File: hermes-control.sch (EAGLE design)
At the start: 73 parts, among them J1 1981568-1, J3 2201778-1, Q2 BC849SMD, Q3 FDN360P, Q4 FDN360P, Q5 BC849SMD, Q6 MMBT3906SOT23-3, Q7 FDN360P, Q8 MMBT2222A, U1 LSM9DS1TR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

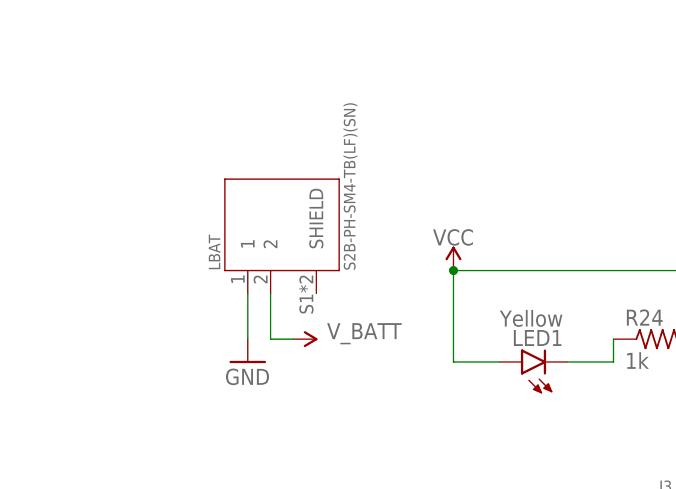
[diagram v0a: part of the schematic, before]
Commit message: new bat connector
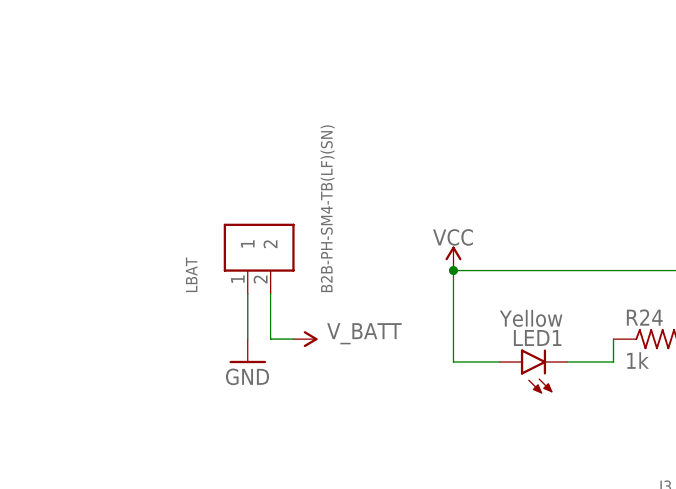
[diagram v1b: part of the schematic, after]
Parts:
- LBAT: value S2B-PH-SM4-TB(LF)(SN) -> B2B-PH-SM4-TB(LF)(SN); device hermes:S2B-PH-SM4-TB(LF)(SN) -> B2B-PH-SM4-TB_LF__SN_:B2B-PH-SM4-TB(LF)(SN)
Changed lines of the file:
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@@
 <part name="J3" library="hermes" deviceset="2201778-1" device=""/>
 <part name="GND13" library="supply1" library_urn="urn:adsk.eagle:library:371" deviceset="GND" device=""/>
-<part name="LBAT" library="hermes" deviceset="S2B-PH-SM4-TB(LF)(SN)" device=""/>
+<part name="LBAT" library="B2B-PH-SM4-TB_LF__SN_" deviceset="B2B-PH-SM4-TB(LF)(SN)" device=""/>
 <part name="SUPPLY22" library="SparkFun-PowerSymbols" library_urn="urn:adsk.eagle:library:530" deviceset="3.3V" device=""/>
 <part name="SUPPLY23" library="SparkFun-PowerSymbols" library_urn="urn:adsk.eagle:library:530" deviceset="3.3V" device=""/>
@@
 <attribute name="VALUE" x="124.46" y="106.68" size="1.778" layer="96"/>
 </instance>
-<instance part="LBAT" gate="G$1" x="50.8" y="172.72" smashed="yes" rot="R90">
-<attribute name="NAME" x="45.20428125" y="167.6371" size="1.272509375" layer="95" rot="R90"/>
-<attribute name="VALUE" x="60.22268125" y="167.63188125" size="1.275409375" layer="96" rot="R90"/>
+<instance part="LBAT" gate="G$1" x="48.26" y="170.18" smashed="yes" rot="R90">
+<attribute name="NAME" x="42.66428125" y="165.0971" size="1.272509375" layer="95" rot="R90"/>
+<attribute name="VALUE" x="57.68268125" y="165.09188125" size="1.275409375" layer="96" rot="R90"/>
 </instance>
 <instance part="SUPPLY22" gate="G$1" x="360.68" y="129.54" smashed="yes">

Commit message: flipped fet
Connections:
- net 3.3V: now also Q3.S; no longer Q3.D
- net N$6: now also Q3.D; no longer Q3.S
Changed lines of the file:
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@@
 <?xml version="1.0" encoding="utf-8"?>
 <!DOCTYPE eagle SYSTEM "eagle.dtd">
-<eagle version="9.4.0">
+<eagle version="9.4.2">
 <drawing>
 <settings>
@@
 <attribute name="VALUE" x="315.595" y="36.068" size="1.778" layer="96" rot="R90"/>
 </instance>
-<instance part="Q3" gate="G$1" x="236.22" y="30.48" smashed="yes" rot="R90">
-<attribute name="NAME" x="233.68" y="36.83" size="1.778" layer="95" rot="R90"/>
-<attribute name="VALUE" x="236.22" y="36.83" size="1.778" layer="96" rot="R90"/>
+<instance part="Q3" gate="G$1" x="236.22" y="30.48" smashed="yes" rot="MR90">
+<attribute name="NAME" x="238.76" y="36.83" size="1.778" layer="95" rot="MR90"/>
+<attribute name="VALUE" x="236.22" y="36.83" size="1.778" layer="96" rot="MR90"/>
 </instance>
 <instance part="C14" gate="G$1" x="218.44" y="30.48" smashed="yes">
@@
 <pinref part="SUPPLY7" gate="G$1" pin="3.3V"/>
 <wire x1="246.38" y1="35.56" x2="246.38" y2="33.02" width="0.1524" layer="91"/>
-<pinref part="Q3" gate="G$1" pin="D"/>
-<wire x1="246.38" y1="33.02" x2="241.3" y2="33.02" width="0.1524" layer="91"/>
+<pinref part="Q3" gate="G$1" pin="S"/>
+<wire x1="241.3" y1="33.02" x2="246.38" y2="33.02" width="0.1524" layer="91"/>
 </segment>
 <segment>
@@
 <pinref part="C7" gate="G$1" pin="1"/>
 <junction x="210.82" y="33.02"/>
-<pinref part="Q3" gate="G$1" pin="S"/>
+<pinref part="Q3" gate="G$1" pin="D"/>
 <wire x1="231.14" y1="33.02" x2="218.44" y2="33.02" width="0.1524" layer="91"/>
 <junction x="218.44" y="33.02"/>
@@
 </segment>
 <segment>
+<wire x1="238.76" y1="27.94" x2="248.92" y2="27.94" width="0.1524" layer="91"/>
+<label x="241.3" y="27.94" size="1.778" layer="95"/>
 <pinref part="Q3" gate="G$1" pin="G"/>
-<wire x1="233.68" y1="27.94" x2="248.92" y2="27.94" width="0.1524" layer="91"/>
-<label x="241.3" y="27.94" size="1.778" layer="95"/>
-</segment>
-</net>
+</segment>
+</net>

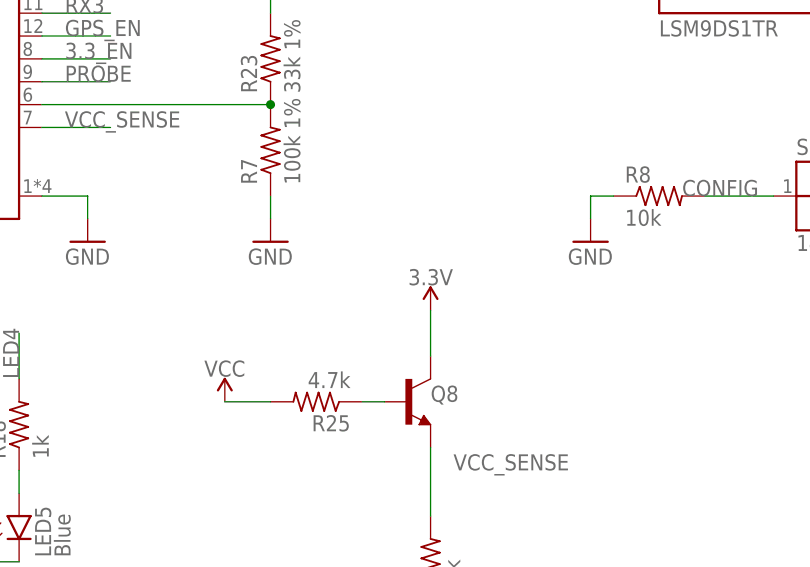
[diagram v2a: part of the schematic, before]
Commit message: changed from 3.3 to vccio
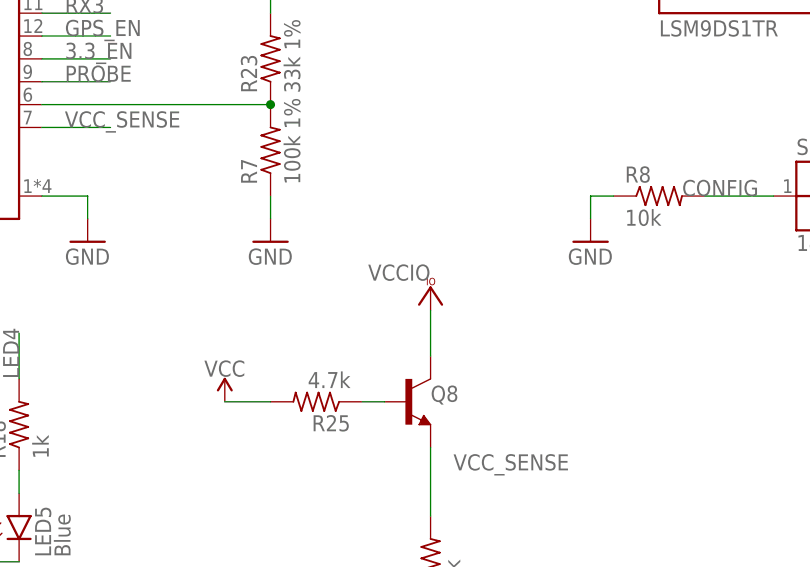
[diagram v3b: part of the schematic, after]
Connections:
- net 3.3V: no longer Q8.C
- net VCCIO: now also Q8.C
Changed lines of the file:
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@@
 <part name="R9" library="rcl" library_urn="urn:adsk.eagle:library:334" deviceset="R-US_" device="R0603" package3d_urn="urn:adsk.eagle:package:23555/3" value="10k"/>
 <part name="R25" library="rcl" library_urn="urn:adsk.eagle:library:334" deviceset="R-US_" device="R0603" package3d_urn="urn:adsk.eagle:package:23555/3" value="4.7k"/>
-<part name="SUPPLY31" library="SparkFun-PowerSymbols" library_urn="urn:adsk.eagle:library:530" deviceset="3.3V" device=""/>
 <part name="GND11" library="supply1" library_urn="urn:adsk.eagle:library:371" deviceset="GND" device=""/>
 <part name="VCC4" library="supply1" library_urn="urn:adsk.eagle:library:371" deviceset="VCCIO" device=""/>
 <part name="VCC5" library="supply1" library_urn="urn:adsk.eagle:library:371" deviceset="VCCIO" device=""/>
 <part name="VCC6" library="supply1" library_urn="urn:adsk.eagle:library:371" deviceset="VCCIO" device=""/>
+<part name="VCC7" library="supply1" library_urn="urn:adsk.eagle:library:371" deviceset="VCCIO" device=""/>
 </parts>
 <sheets>
@@
 <attribute name="VALUE" x="346.71" y="56.642" size="1.778" layer="96" rot="R180"/>
 </instance>
-<instance part="SUPPLY31" gate="G$1" x="355.6" y="63.5" smashed="yes">
-<attribute name="VALUE" x="355.6" y="66.294" size="1.778" layer="96" align="bottom-center"/>
-</instance>
 <instance part="GND11" gate="1" x="355.6" y="25.4" smashed="yes">
 <attribute name="VALUE" x="353.06" y="22.86" size="1.778" layer="96"/>
@@
 <instance part="VCC6" gate="G$1" x="129.54" y="147.32" smashed="yes">
 <attribute name="VALUE" x="129.54" y="149.86" size="1.778" layer="96" rot="R180"/>
+</instance>
+<instance part="VCC7" gate="G$1" x="355.6" y="66.04" smashed="yes">
+<attribute name="VALUE" x="355.6" y="68.58" size="1.778" layer="96" rot="R180"/>
 </instance>
 </instances>
@@
 <wire x1="228.6" y1="81.28" x2="228.6" y2="83.82" width="0.1524" layer="91"/>
 </segment>
-<segment>
-<pinref part="Q8" gate="&gt;NAME" pin="C"/>
-<pinref part="SUPPLY31" gate="G$1" pin="3.3V"/>
-<wire x1="355.6" y1="58.42" x2="355.6" y2="63.5" width="0.1524" layer="91"/>
-</segment>
 </net>
 <net name="N$4" class="0">
@@
 <wire x1="129.54" y1="139.7" x2="124.46" y2="139.7" width="0.1524" layer="91"/>
 </segment>
-</net>
+<segment>
+<pinref part="Q8" gate="&gt;NAME" pin="C"/>
+<wire x1="355.6" y1="58.42" x2="355.6" y2="63.5" width="0.1524" layer="91"/>
+<pinref part="VCC7" gate="G$1" pin="VCCIO"/>
+</segment>
+</net>

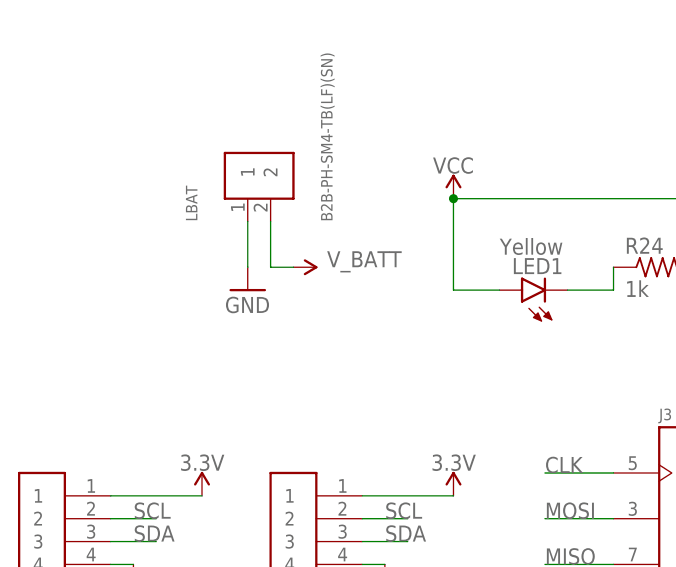
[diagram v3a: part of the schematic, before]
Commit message: changed batt connection
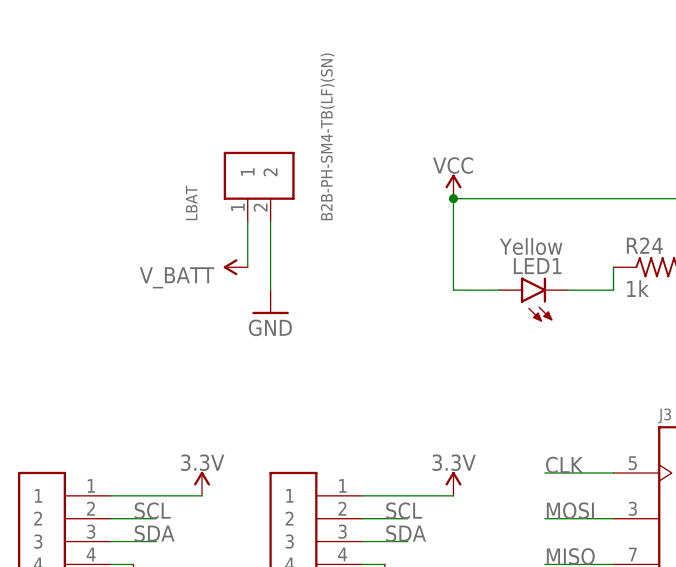
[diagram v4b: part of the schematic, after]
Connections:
- net GND: now also LBAT.2; no longer LBAT.1
- net V_BATT: now also LBAT.1; no longer LBAT.2
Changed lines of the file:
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@@
 <attribute name="VALUE" x="233.68" y="149.86" size="1.778" layer="96"/>
 </instance>
-<instance part="GND7" gate="1" x="48.26" y="157.48" smashed="yes">
-<attribute name="VALUE" x="45.72" y="154.94" size="1.778" layer="96"/>
-</instance>
-<instance part="SUPPLY6" gate="G$1" x="53.34" y="160.02" smashed="yes" rot="R270">
-<attribute name="VALUE" x="61.214" y="160.02" size="1.778" layer="96" align="bottom-center"/>
+<instance part="GND7" gate="1" x="50.8" y="154.94" smashed="yes">
+<attribute name="VALUE" x="48.26" y="152.4" size="1.778" layer="96"/>
+</instance>
+<instance part="SUPPLY6" gate="G$1" x="48.26" y="160.02" smashed="yes" rot="R90">
+<attribute name="VALUE" x="40.386" y="160.02" size="1.778" layer="96" rot="R180" align="bottom-center"/>
 </instance>
 <instance part="GND8" gate="1" x="200.66" y="17.78" smashed="yes">
@@
 </segment>
 <segment>
-<pinref part="GND7" gate="1" pin="GND"/>
-<wire x1="48.26" y1="160.02" x2="48.26" y2="165.1" width="0.1524" layer="91"/>
-<pinref part="LBAT" gate="G$1" pin="1"/>
-</segment>
-<segment>
 <pinref part="GND12" gate="1" pin="GND"/>
 <wire x1="147.32" y1="99.06" x2="147.32" y2="101.6" width="0.1524" layer="91"/>
@@
 <wire x1="129.54" y1="35.56" x2="137.16" y2="35.56" width="0.1524" layer="91"/>
 </segment>
+<segment>
+<pinref part="GND7" gate="1" pin="GND"/>
+<pinref part="LBAT" gate="G$1" pin="2"/>
+<wire x1="50.8" y1="157.48" x2="50.8" y2="165.1" width="0.1524" layer="91"/>
+</segment>
 </net>
 <net name="N$1" class="0">
@@
 </segment>
 <segment>
-<pinref part="SUPPLY6" gate="G$1" pin="V_BATT"/>
-<wire x1="53.34" y1="160.02" x2="50.8" y2="160.02" width="0.1524" layer="91"/>
-<wire x1="50.8" y1="160.02" x2="50.8" y2="165.1" width="0.1524" layer="91"/>
-<pinref part="LBAT" gate="G$1" pin="2"/>
-</segment>
-<segment>
 <pinref part="SUPPLY13" gate="G$1" pin="V_BATT"/>
 <wire x1="337.82" y1="99.06" x2="337.82" y2="96.52" width="0.1524" layer="91"/>
@@
 <wire x1="213.36" y1="172.72" x2="218.44" y2="172.72" width="0.1524" layer="91"/>
 </segment>
+<segment>
+<pinref part="SUPPLY6" gate="G$1" pin="V_BATT"/>
+<pinref part="LBAT" gate="G$1" pin="1"/>
+<wire x1="48.26" y1="160.02" x2="48.26" y2="165.1" width="0.1524" layer="91"/>
+</segment>
 </net>

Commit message: more vccio
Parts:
- added R5: 10k, rcl:R-US_R0603
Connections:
- net 3.3V: no longer R12.2, R13.2, S2.2
- net 3.3_EN: now also R5.1
- net VCCIO: now also R12.2, R13.2, R5.2, S2.2
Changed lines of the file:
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@@
 <?xml version="1.0" encoding="utf-8"?>
 <!DOCTYPE eagle SYSTEM "eagle.dtd">
-<eagle version="9.4.2">
+<eagle version="9.3.0">
 <drawing>
 <settings>
@@
 <part name="SUPPLY13" library="SparkFun-PowerSymbols" library_urn="urn:adsk.eagle:library:530" deviceset="V_BATT" device=""/>
 <part name="GND14" library="supply1" library_urn="urn:adsk.eagle:library:371" deviceset="GND" device=""/>
-<part name="SUPPLY14" library="SparkFun-PowerSymbols" library_urn="urn:adsk.eagle:library:530" deviceset="3.3V" device=""/>
 <part name="GND15" library="supply1" library_urn="urn:adsk.eagle:library:371" deviceset="GND" device=""/>
 <part name="U$3" library="BlueRobotics-JST-GH" deviceset="JST-GH-4" device="TOP"/>
@@
 <part name="R6" library="rcl" library_urn="urn:adsk.eagle:library:334" deviceset="R-US_" device="R0603" package3d_urn="urn:adsk.eagle:package:23555/3" value="1k"/>
 <part name="R12" library="rcl" library_urn="urn:adsk.eagle:library:334" deviceset="R-US_" device="R0603" package3d_urn="urn:adsk.eagle:package:23555/3" value="1k"/>
-<part name="SUPPLY26" library="SparkFun-PowerSymbols" library_urn="urn:adsk.eagle:library:530" deviceset="3.3V" device=""/>
 <part name="R13" library="rcl" library_urn="urn:adsk.eagle:library:334" deviceset="R-US_" device="R0603" package3d_urn="urn:adsk.eagle:package:23555/3" value="27k"/>
 <part name="R14" library="rcl" library_urn="urn:adsk.eagle:library:334" deviceset="R-US_" device="R0603" package3d_urn="urn:adsk.eagle:package:23555/3" value="10k"/>
@@
 <part name="VCC6" library="supply1" library_urn="urn:adsk.eagle:library:371" deviceset="VCCIO" device=""/>
 <part name="VCC7" library="supply1" library_urn="urn:adsk.eagle:library:371" deviceset="VCCIO" device=""/>
+<part name="VCC8" library="supply1" library_urn="urn:adsk.eagle:library:371" deviceset="VCCIO" device=""/>
+<part name="VCC9" library="supply1" library_urn="urn:adsk.eagle:library:371" deviceset="VCCIO" device=""/>
+<part name="R5" library="rcl" library_urn="urn:adsk.eagle:library:334" deviceset="R-US_" device="R0603" package3d_urn="urn:adsk.eagle:package:23555/3" value="10k"/>
 </parts>
 <sheets>
@@
 <attribute name="VALUE" x="71.12" y="170.434" size="1.778" layer="96" align="bottom-center"/>
 </instance>
-<instance part="SUPPLY3" gate="G$1" x="304.8" y="185.42" smashed="yes">
-<attribute name="VALUE" x="304.8" y="188.214" size="1.778" layer="96" align="bottom-center"/>
+<instance part="SUPPLY3" gate="G$1" x="304.8" y="182.88" smashed="yes">
+<attribute name="VALUE" x="304.8" y="185.674" size="1.778" layer="96" align="bottom-center"/>
 </instance>
 <instance part="SUPPLY4" gate="G$1" x="213.36" y="172.72" smashed="yes">
@@
 <instance part="GND14" gate="1" x="337.82" y="71.12" smashed="yes">
 <attribute name="VALUE" x="335.28" y="68.58" size="1.778" layer="96"/>
-</instance>
-<instance part="SUPPLY14" gate="G$1" x="421.64" y="76.2" smashed="yes">
-<attribute name="VALUE" x="421.64" y="78.994" size="1.778" layer="96" align="bottom-center"/>
 </instance>
 <instance part="GND15" gate="1" x="279.4" y="30.48" smashed="yes">
@@
 <attribute name="VALUE" x="117.602" y="87.63" size="1.778" layer="96" rot="R90"/>
 </instance>
-<instance part="SUPPLY26" gate="G$1" x="114.3" y="99.06" smashed="yes">
-<attribute name="VALUE" x="114.3" y="101.854" size="1.778" layer="96" align="bottom-center"/>
-</instance>
 <instance part="R13" gate="G$1" x="106.68" y="86.36" smashed="yes" rot="R90">
 <attribute name="NAME" x="105.1814" y="82.55" size="1.778" layer="95" rot="R90"/>
@@
 <attribute name="VALUE" x="313.182" y="46.99" size="1.778" layer="96" rot="R90"/>
 </instance>
-<instance part="VCC1" gate="G$1" x="314.96" y="187.96" smashed="yes">
-<attribute name="VALUE" x="317.5" y="185.42" size="1.778" layer="96" rot="R270"/>
+<instance part="VCC1" gate="G$1" x="314.96" y="195.58" smashed="yes">
+<attribute name="VALUE" x="317.5" y="193.04" size="1.778" layer="96" rot="R270"/>
 </instance>
 <instance part="VCC2" gate="G$1" x="322.58" y="149.86" smashed="yes">
@@
 <instance part="VCC7" gate="G$1" x="355.6" y="66.04" smashed="yes">
 <attribute name="VALUE" x="355.6" y="68.58" size="1.778" layer="96" rot="R180"/>
+</instance>
+<instance part="VCC8" gate="G$1" x="114.3" y="104.14" smashed="yes">
+<attribute name="VALUE" x="114.3" y="106.68" size="1.778" layer="96" rot="R180"/>
+</instance>
+<instance part="VCC9" gate="G$1" x="421.64" y="81.28" smashed="yes">
+<attribute name="VALUE" x="421.64" y="83.82" size="1.778" layer="96" rot="R180"/>
+</instance>
+<instance part="R5" gate="G$1" x="304.8" y="190.5" smashed="yes">
+<attribute name="NAME" x="300.99" y="191.9986" size="1.778" layer="95"/>
+<attribute name="VALUE" x="300.99" y="187.198" size="1.778" layer="96"/>
 </instance>
 </instances>
@@
 <pinref part="SUPPLY21" gate="G$1" pin="3.3V"/>
 <wire x1="55.88" y1="27.94" x2="66.04" y2="27.94" width="0.1524" layer="91"/>
-</segment>
-<segment>
-<pinref part="SUPPLY14" gate="G$1" pin="3.3V"/>
-<pinref part="S2" gate="G$1" pin="2"/>
-<wire x1="421.64" y1="76.2" x2="411.48" y2="76.2" width="0.1524" layer="91"/>
 </segment>
 <segment>
@@
 </segment>
 <segment>
-<pinref part="R12" gate="G$1" pin="2"/>
-<pinref part="SUPPLY26" gate="G$1" pin="3.3V"/>
-<wire x1="114.3" y1="96.52" x2="114.3" y2="99.06" width="0.1524" layer="91"/>
-<pinref part="R13" gate="G$1" pin="2"/>
-<wire x1="106.68" y1="91.44" x2="106.68" y2="96.52" width="0.1524" layer="91"/>
-<wire x1="106.68" y1="96.52" x2="114.3" y2="96.52" width="0.1524" layer="91"/>
-<junction x="114.3" y="96.52"/>
-</segment>
-<segment>
 <pinref part="SUPPLY3" gate="G$1" pin="3.3V"/>
-<wire x1="304.8" y1="182.88" x2="304.8" y2="185.42" width="0.1524" layer="91"/>
 <pinref part="Q7" gate="G$1" pin="D"/>
 </segment>
@@
 <junction x="304.8" y="172.72"/>
 <wire x1="304.8" y1="172.72" x2="314.96" y2="172.72" width="0.1524" layer="91"/>
-<wire x1="314.96" y1="172.72" x2="314.96" y2="185.42" width="0.1524" layer="91"/>
+<wire x1="314.96" y1="172.72" x2="314.96" y2="190.5" width="0.1524" layer="91"/>
 <pinref part="VCC1" gate="G$1" pin="VCCIO"/>
 <pinref part="Q7" gate="G$1" pin="S"/>
+<pinref part="R5" gate="G$1" pin="2"/>
+<wire x1="314.96" y1="190.5" x2="314.96" y2="193.04" width="0.1524" layer="91"/>
+<wire x1="309.88" y1="190.5" x2="314.96" y2="190.5" width="0.1524" layer="91"/>
+<junction x="314.96" y="190.5"/>
 </segment>
 <segment>
@@
 <pinref part="VCC7" gate="G$1" pin="VCCIO"/>
 </segment>
+<segment>
+<pinref part="R12" gate="G$1" pin="2"/>
+<pinref part="R13" gate="G$1" pin="2"/>
+<wire x1="106.68" y1="91.44" x2="106.68" y2="96.52" width="0.1524" layer="91"/>
+<wire x1="106.68" y1="96.52" x2="114.3" y2="96.52" width="0.1524" layer="91"/>
+<junction x="114.3" y="96.52"/>
+<pinref part="VCC8" gate="G$1" pin="VCCIO"/>
+<wire x1="114.3" y1="101.6" x2="114.3" y2="96.52" width="0.1524" layer="91"/>
+</segment>
+<segment>
+<pinref part="S2" gate="G$1" pin="2"/>
+<wire x1="421.64" y1="76.2" x2="411.48" y2="76.2" width="0.1524" layer="91"/>
+<pinref part="VCC9" gate="G$1" pin="VCCIO"/>
+<wire x1="421.64" y1="78.74" x2="421.64" y2="76.2" width="0.1524" layer="91"/>
+</segment>
 </net>
 <net name="TX0" class="0">
@@
 </segment>
 <segment>
-<wire x1="299.72" y1="175.26" x2="299.72" y2="193.04" width="0.1524" layer="91"/>
-<label x="299.72" y="193.04" size="1.778" layer="95"/>
+<wire x1="299.72" y1="175.26" x2="299.72" y2="190.5" width="0.1524" layer="91"/>
+<label x="299.72" y="195.58" size="1.778" layer="95"/>
 <pinref part="Q7" gate="G$1" pin="G"/>
-</segment>
-</net>
+<pinref part="R5" gate="G$1" pin="1"/>
+<wire x1="299.72" y1="190.5" x2="299.72" y2="195.58" width="0.1524" layer="91"/>
+<junction x="299.72" y="190.5"/>
+</segment>
+</net>
